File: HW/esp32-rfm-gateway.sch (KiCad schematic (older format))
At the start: 59 parts, among them J1 Res, J2 Boot, J20 220V~, J21 c5V, J22 s14500, J23 s18650, J24 cPS, J25 c3V3, J3 PinDbg, J30 AntSMA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

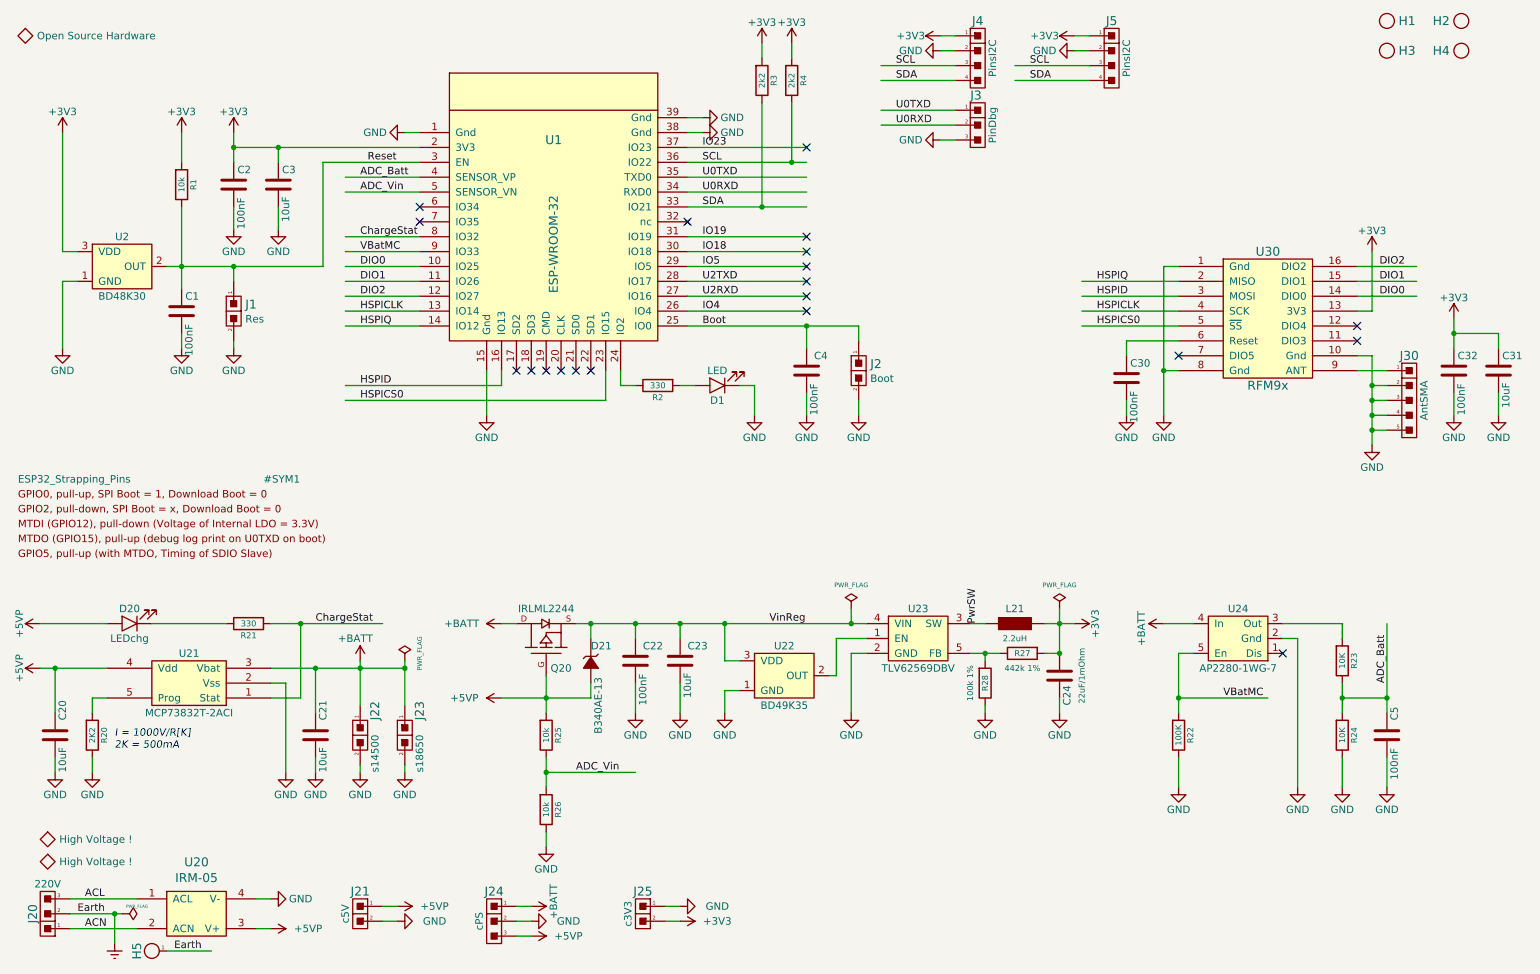
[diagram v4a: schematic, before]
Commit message: Rebuilds the power sections, again ...
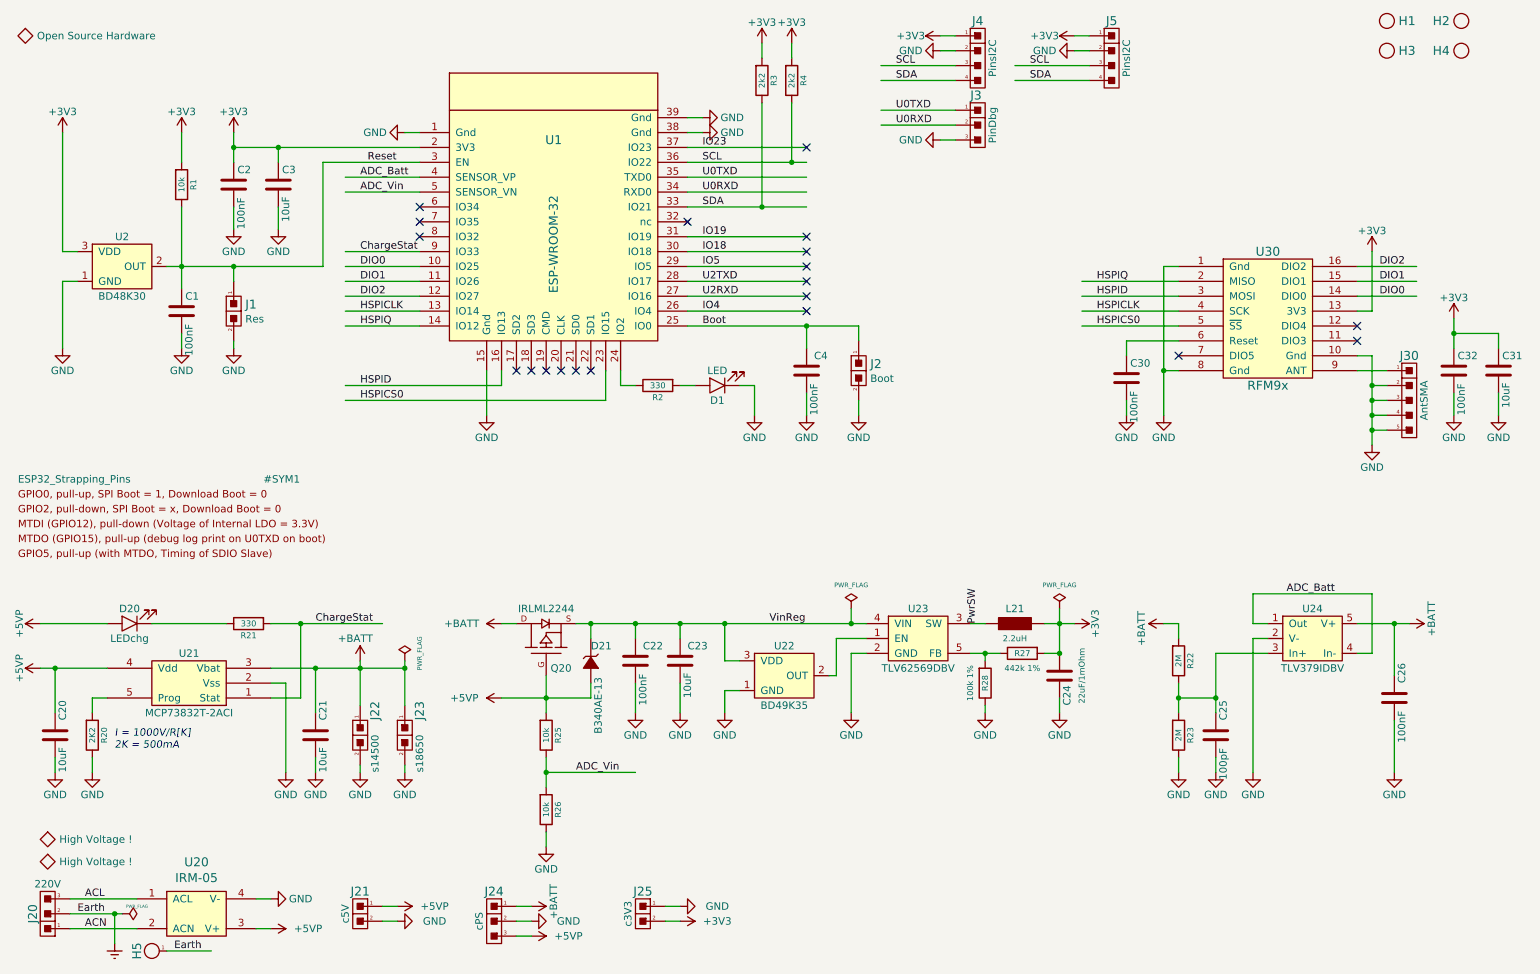
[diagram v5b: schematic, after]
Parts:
- removed R24: 10K, CalinGeneric:R0805HS, symbol calin:R
- removed U24: AP2280-1WG-7, CalinGeneric:SOT-23-5-HS, symbol calin:AP2280-1WG-7
- added C25: 100pF, CalinGeneric:C0805HS, symbol Device:C
- added U24: TLV379IDBV, CalinGeneric:SOT-23-5-HS, symbol calin:TLV379IDBV
- R22: value 100K -> 2M
- R23: value 10K -> 2M
- renumbered C5 to C26
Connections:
- net labels removed: VBatMC
- wire segments 211 -> 214
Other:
- moved on the sheet: C26, R22, R23
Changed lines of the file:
@@
 Title "ESP32 RFM69/RFM9x Gateway"
 Date "2019-04-13"
-Rev "16"
+Rev "17"
 Comp "Calin Radoni"
 Comment1 ""
@@
 	1950 2500 1950 2650
 $Comp
-L calin:R R24
-U 1 1 5C35D5DE
-P 9750 5650
-F 0 "R24" V 9830 5650 40  0000 C CNN
-F 1 "10K" V 9750 5650 40  0000 C CNN
-F 2 "CalinGeneric:R0805HS" V 9680 5650 30  0001 C CNN
-F 3 "" H 9750 5650 30  0000 C CNN
-	1    9750 5650
-	1    0    0    -1
-$EndComp
-$Comp
 L calin:R R23
 U 1 1 5C35D656
-P 9750 5150
-F 0 "R23" V 9830 5150 40  0000 C CNN
-F 1 "10K" V 9750 5150 40  0000 C CNN
-F 2 "CalinGeneric:R0805HS" V 9680 5150 30  0001 C CNN
-F 3 "" H 9750 5150 30  0000 C CNN
-	1    9750 5150
+P 8650 5650
+F 0 "R23" V 8730 5650 40  0000 C CNN
+F 1 "2M" V 8650 5650 40  0000 C CNN
+F 2 "CalinGeneric:R0805HS" V 8580 5650 30  0001 C CNN
+F 3 "" H 8650 5650 30  0000 C CNN
+	1    8650 5650
 	1    0    0    -1
 $EndComp
@@
 	0    -1   -1   0
 $EndComp
-$Comp
-L power:GND #PWR0114
-U 1 1 5C35D729
-P 9750 6000
-F 0 "#PWR0114" H 9750 5750 50  0001 C CNN
-F 1 "GND" H 9750 5850 50  0000 C CNN
-F 2 "" H 9750 6000 50  0000 C CNN
-F 3 "" H 9750 6000 50  0000 C CNN
-	1    9750 6000
-	1    0    0    -1
-$EndComp
-Wire Wire Line
-	9750 5800 9750 6000
-Text Label 10050 5300 1    50   ~ 0
+Text Label 9700 4700 2    50   ~ 0
 ADC_Batt
 Wire Wire Line
@@
 	1    0    0    -1
 $EndComp
-Wire Wire Line
-	3550 2300 3050 2300
 $Comp
 L calin:LED D1
@@
 L power:GND #PWR0125
 U 1 1 5C64E70C
-P 9450 6000
-F 0 "#PWR0125" H 9450 5750 50  0001 C CNN
-F 1 "GND" H 9450 5850 50  0000 C CNN
-F 2 "" H 9450 6000 50  0000 C CNN
-F 3 "" H 9450 6000 50  0000 C CNN
-	1    9450 6000
+P 9150 5900
+F 0 "#PWR0125" H 9150 5650 50  0001 C CNN
+F 1 "GND" H 9150 5750 50  0000 C CNN
+F 2 "" H 9150 5900 50  0000 C CNN
+F 3 "" H 9150 5900 50  0000 C CNN
+	1    9150 5900
 	1    0    0    -1
 $EndComp
@@
 L calin:R R22
 U 1 1 5C6A9C35
-P 8650 5650
-F 0 "R22" V 8730 5650 40  0000 C CNN
-F 1 "100K" V 8650 5650 40  0000 C CNN
-F 2 "CalinGeneric:R0805HS" V 8580 5650 30  0001 C CNN
-F 3 "" H 8650 5650 30  0000 C CNN
-	1    8650 5650
+P 8650 5150
+F 0 "R22" V 8730 5150 40  0000 C CNN
+F 1 "2M" V 8650 5150 40  0000 C CNN
+F 2 "CalinGeneric:R0805HS" V 8580 5150 30  0001 C CNN
+F 3 "" H 8650 5150 30  0000 C CNN
+	1    8650 5150
 	1    0    0    -1
 $EndComp
@@
 L power:GND #PWR0126
 U 1 1 5C68E455
-P 8650 6000
-F 0 "#PWR0126" H 8650 5750 50  0001 C CNN
-F 1 "GND" H 8650 5850 50  0000 C CNN
-F 2 "" H 8650 6000 50  0000 C CNN
-F 3 "" H 8650 6000 50  0000 C CNN
-	1    8650 6000
-	1    0    0    -1
-$EndComp
-Wire Wire Line
-	8650 5800 8650 6000
-$Comp
-L calin:AP2280-1WG-7 U24
-U 1 1 5C6B0532
-P 9050 5000
-F 0 "U24" H 9050 4800 50  0000 C CNN
-F 1 "AP2280-1WG-7" H 9050 5200 50  0000 C CNN
-F 2 "CalinGeneric:SOT-23-5-HS" H 9050 5000 50  0001 C CNN
-F 3 "" H 9050 5000 50  0001 C CNN
-	1    9050 5000
-	-1   0    0    1
-$EndComp
-NoConn ~ 9350 5100
-Wire Wire Line
-	9350 4900 9750 4900
-Wire Wire Line
-	9750 4900 9750 5000
-Wire Wire Line
-	9350 5000 9450 5000
-Wire Wire Line
-	9450 5000 9450 6000
-Wire Wire Line
-	8750 5100 8650 5100
-Wire Wire Line
-	8650 5100 8650 5400
-Wire Wire Line
-	8750 4900 8550 4900
-Wire Wire Line
-	8650 5400 9250 5400
-Connection ~ 8650 5400
-Wire Wire Line
-	8650 5400 8650 5500
-Text Label 8950 5400 0    50   ~ 0
-VBatMC
+P 8650 5900
+F 0 "#PWR0126" H 8650 5650 50  0001 C CNN
+F 1 "GND" H 8650 5750 50  0000 C CNN
+F 2 "" H 8650 5900 50  0000 C CNN
+F 3 "" H 8650 5900 50  0000 C CNN
+	1    8650 5900
+	1    0    0    -1
+$EndComp
 $Comp
 L calin:BD49K U22
@@
 Text Label 6750 1550 0    50   ~ 0
 U0RXD
-Text Label 3150 2400 0    50   ~ 0
-VBatMC
 Wire Wire Line
 	10050 3300 9950 3300
@@
 	9950 3600 9950 3500
 $Comp
-L Device:C C5
+L Device:C C26
 U 1 1 5CD11338
-P 10050 5650
-F 0 "C5" V 10100 5750 50  0000 L CNN
-F 1 "100nF" V 10100 5350 50  0000 L CNN
-F 2 "CalinGeneric:C0805HS" H 10088 5500 50  0001 C CNN
-F 3 "" H 10050 5650 50  0000 C CNN
-	1    10050 5650
-	1    0    0    -1
-$EndComp
-$Comp
-L power:GND #PWR0140
-U 1 1 5CD113F8
-P 10050 6000
-F 0 "#PWR0140" H 10050 5750 50  0001 C CNN
-F 1 "GND" H 10050 5850 50  0000 C CNN
-F 2 "" H 10050 6000 50  0000 C CNN
-F 3 "" H 10050 6000 50  0000 C CNN
-	1    10050 6000
-	1    0    0    -1
-$EndComp
-Wire Wire Line
-	10050 6000 10050 5800
-Wire Wire Line
-	9750 5300 9750 5400
-Wire Wire Line
-	10050 5500 10050 5400
-Wire Wire Line
-	10050 5400 9750 5400
-Connection ~ 9750 5400
-Wire Wire Line
-	9750 5400 9750 5500
-Wire Wire Line
-	10050 5400 10050 4900
-Connection ~ 10050 5400
+P 10100 5400
+F 0 "C26" V 10150 5500 50  0000 L CNN
+F 1 "100nF" V 10150 5100 50  0000 L CNN
+F 2 "CalinGeneric:C0805HS" H 10138 5250 50  0001 C CNN
+F 3 "" H 10100 5400 50  0000 C CNN
+	1    10100 5400
+	1    0    0    -1
+$EndComp
 $Comp
 L calin:CS_3 J20
@@
 Text Label 2850 4900 0    50   ~ 0
 ChargeStat
-Text Label 3150 2300 0    50   ~ 0
-ChargeStat
 $Comp
 L power:PWR_FLAG #FLG0101
@@
 NoConn ~ 3550 2100
 NoConn ~ 3550 2200
+$Comp
+L calin:TLV379IDBV U24
+U 1 1 5CB3BC97
+P 9550 5000
+F 0 "U24" H 9550 5200 50  0000 C CNN
+F 1 "TLV379IDBV" H 9550 4800 50  0000 C CNN
+F 2 "CalinGeneric:SOT-23-5-HS" H 9550 5000 50  0001 C CNN
+F 3 "" H 9550 5000 50  0001 C CNN
+	1    9550 5000
+	1    0    0    -1
+$EndComp
+Wire Wire Line
+	9250 4900 9150 4900
+Wire Wire Line
+	9150 4900 9150 4700
+Wire Wire Line
+	9150 4700 9950 4700
+Wire Wire Line
+	9950 4700 9950 5100
+Wire Wire Line
+	9950 5100 9850 5100
+$Comp
+L Device:C C25
+U 1 1 5CC0DFEC
+P 8900 5650
+F 0 "C25" V 8950 5750 50  0000 L CNN
+F 1 "100pF" V 8950 5350 50  0000 L CNN
+F 2 "CalinGeneric:C0805HS" H 8938 5500 50  0001 C CNN
+F 3 "" H 8900 5650 50  0000 C CNN
+	1    8900 5650
+	1    0    0    -1
+$EndComp
+$Comp
+L power:+BATT #PWR0114
+U 1 1 5CC18EFD
+P 10200 4900
+F 0 "#PWR0114" H 10200 4750 50  0001 C CNN
+F 1 "+BATT" H 10050 5050 50  0000 L CNN
+F 2 "" H 10200 4900 50  0001 C CNN
+F 3 "" H 10200 4900 50  0001 C CNN
+	1    10200 4900
+	0    1    1    0
+$EndComp
+$Comp
+L power:GND #PWR0140
+U 1 1 5CC1963B
+P 8900 5900
+F 0 "#PWR0140" H 8900 5650 50  0001 C CNN
+F 1 "GND" H 8900 5750 50  0000 C CNN
+F 2 "" H 8900 5900 50  0000 C CNN
+F 3 "" H 8900 5900 50  0000 C CNN
+	1    8900 5900
+	1    0    0    -1
+$EndComp
+$Comp
+L power:GND #PWR0149
+U 1 1 5CC19822
+P 10100 5900
+F 0 "#PWR0149" H 10100 5650 50  0001 C CNN
+F 1 "GND" H 10100 5750 50  0000 C CNN
+F 2 "" H 10100 5900 50  0000 C CNN
+F 3 "" H 10100 5900 50  0000 C CNN
+	1    10100 5900
+	1    0    0    -1
+$EndComp
+Wire Wire Line
+	8550 4900 8650 4900
+Wire Wire Line
+	8650 4900 8650 5000
+Wire Wire Line
+	8650 5300 8650 5400
+Wire Wire Line
+	8650 5800 8650 5900
+Wire Wire Line
+	8900 5800 8900 5900
+Wire Wire Line
+	8650 5400 8900 5400
+Wire Wire Line
+	8900 5400 8900 5500
+Connection ~ 8650 5400
+Wire Wire Line
+	8650 5400 8650 5500
+Wire Wire Line
+	9250 5000 9150 5000
+Wire Wire Line
+	9150 5000 9150 5900
+Wire Wire Line
+	9850 4900 10100 4900
+Wire Wire Line
+	10100 5250 10100 4900
+Connection ~ 10100 4900
+Wire Wire Line
+	10100 4900 10200 4900
+Wire Wire Line
+	10100 5550 10100 5900
+Wire Wire Line
+	9250 5100 8900 5100
+Wire Wire Line
+	8900 5100 8900 5400
+Connection ~ 8900 5400
+Text Label 3150 2400 0    50   ~ 0
+ChargeStat
+NoConn ~ 3550 2300
 $EndSCHEMATC

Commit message: Changes the power connector to SMD pins
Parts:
- H5: footprint CalinGeneric:HolePlated-M2.5 -> CalinConnectors:SMD_Pins_Big_1x1
- J20: footprint CalinConnectors:DG301-5-3 -> CalinConnectors:SMD_Pins_Big_1x3
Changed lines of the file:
@@
 Sheet 1 1
 Title "ESP32 RFM69/RFM9x Gateway"
-Date "2019-04-13"
-Rev "17"
+Date "2019-04-14"
+Rev "18"
 Comp "Calin Radoni"
 Comment1 ""
@@
 F 0 "J20" V 1150 6850 60  0000 C CNN
 F 1 "220V~" H 1050 6650 50  0000 C CNN
-F 2 "CalinConnectors:DG301-5-3" H 1050 6950 60  0001 C CNN
+F 2 "CalinConnectors:SMD_Pins_Big_1x3" H 1050 6950 60  0001 C CNN
 F 3 "" H 1050 6950 60  0000 C CNN
 	1    1050 6850
@@
 F 0 "H5" H 1750 7200 60  0000 C CNN
 F 1 "HolePlated" H 1750 7000 60  0001 C CNN
-F 2 "CalinGeneric:HolePlated-M2.5" H 1750 7100 60  0001 C CNN
+F 2 "CalinConnectors:SMD_Pins_Big_1x1" H 1750 7100 60  0001 C CNN
 F 3 "" H 1750 7100 60  0000 C CNN
 	1    1750 7100

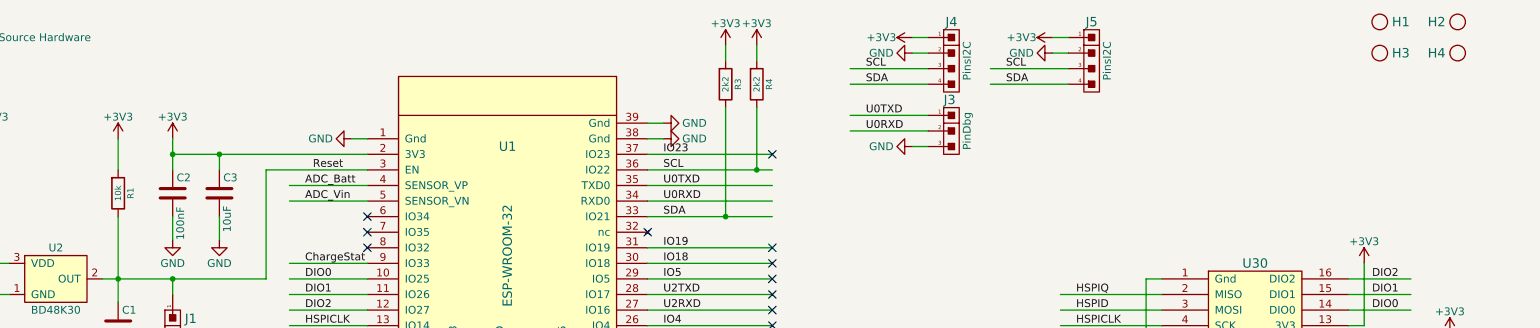
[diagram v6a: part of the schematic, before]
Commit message: Adds CryptoAuthentication device and connects a few more traces
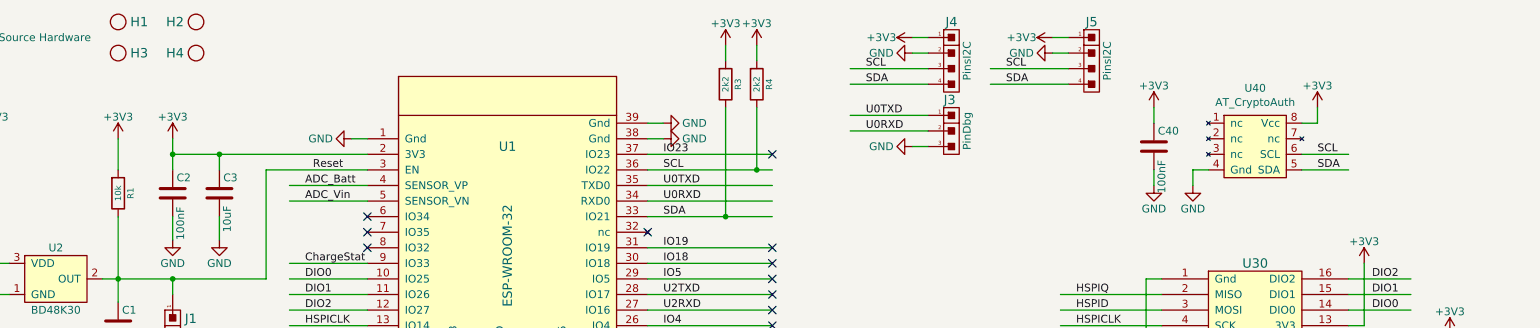
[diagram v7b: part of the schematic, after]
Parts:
- added C40: 100nF, CalinGeneric:C0805HS, symbol Device:C
- added U40: AT_CryptoAuth, CalinGeneric:SOIC-8-HS, symbol calin:AT_CryptoAuth
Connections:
- wire segments 214 -> 222
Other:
- moved on the sheet: H1, H2, H3, H4
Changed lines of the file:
@@
 Title "ESP32 RFM69/RFM9x Gateway"
 Date "2019-04-14"
-Rev "18"
+Rev "19"
 Comp "Calin Radoni"
 Comment1 ""
@@
 L calin:Hole H1
 U 1 1 5C169D3F
-P 10050 850
-F 0 "H1" H 10128 850 60  0000 L CNN
-F 1 "Hole" H 10150 800 60  0001 C CNN
-F 2 "CalinGeneric:HoleNPT-M2.5" H 10050 850 60  0001 C CNN
-F 3 "" H 10050 850 60  0000 C CNN
-	1    10050 850
+P 1950 850
+F 0 "H1" H 2028 850 60  0000 L CNN
+F 1 "Hole" H 2050 800 60  0001 C CNN
+F 2 "CalinGeneric:HoleNPT-M2.5" H 1950 850 60  0001 C CNN
+F 3 "" H 1950 850 60  0000 C CNN
+	1    1950 850
 	1    0    0    -1
 $EndComp
@@
 L calin:Hole H2
 U 1 1 5C169F65
-P 10550 850
-F 0 "H2" H 10628 850 60  0000 L CNN
-F 1 "Hole" H 10650 800 60  0001 C CNN
-F 2 "CalinGeneric:HoleNPT-M2.5" H 10550 850 60  0001 C CNN
-F 3 "" H 10550 850 60  0000 C CNN
-	1    10550 850
+P 2450 850
+F 0 "H2" H 2528 850 60  0000 L CNN
+F 1 "Hole" H 2550 800 60  0001 C CNN
+F 2 "CalinGeneric:HoleNPT-M2.5" H 2450 850 60  0001 C CNN
+F 3 "" H 2450 850 60  0000 C CNN
+	1    2450 850
 	-1   0    0    -1
 $EndComp
@@
 L calin:Hole H3
 U 1 1 5CB3F287
-P 10050 1050
-F 0 "H3" H 10128 1050 60  0000 L CNN
-F 1 "Hole" H 10150 1000 60  0001 C CNN
-F 2 "CalinGeneric:HoleNPT-M2.5" H 10050 1050 60  0001 C CNN
-F 3 "" H 10050 1050 60  0000 C CNN
-	1    10050 1050
+P 1950 1050
+F 0 "H3" H 2028 1050 60  0000 L CNN
+F 1 "Hole" H 2050 1000 60  0001 C CNN
+F 2 "CalinGeneric:HoleNPT-M2.5" H 1950 1050 60  0001 C CNN
+F 3 "" H 1950 1050 60  0000 C CNN
+	1    1950 1050
 	1    0    0    -1
 $EndComp
@@
 L calin:Hole H4
 U 1 1 5CB3F28D
-P 10550 1050
-F 0 "H4" H 10628 1050 60  0000 L CNN
-F 1 "Hole" H 10650 1000 60  0001 C CNN
-F 2 "CalinGeneric:HoleNPT-M2.5" H 10550 1050 60  0001 C CNN
-F 3 "" H 10550 1050 60  0000 C CNN
-	1    10550 1050
+P 2450 1050
+F 0 "H4" H 2528 1050 60  0000 L CNN
+F 1 "Hole" H 2550 1000 60  0001 C CNN
+F 2 "CalinGeneric:HoleNPT-M2.5" H 2450 1050 60  0001 C CNN
+F 3 "" H 2450 1050 60  0000 C CNN
+	1    2450 1050
 	-1   0    0    -1
 $EndComp
@@
 ChargeStat
 NoConn ~ 3550 2300
+$Comp
+L calin:AT_CryptoAuth U40
+U 1 1 5CB52A4F
+P 9250 1650
+F 0 "U40" H 9250 2025 50  0000 C CNN
+F 1 "AT_CryptoAuth" H 9250 1934 50  0000 C CNN
+F 2 "CalinGeneric:SOIC-8-HS" H 9250 1650 50  0001 C CNN
+F 3 "" H 9250 1650 50  0001 C CNN
+	1    9250 1650
+	1    0    0    -1
+$EndComp
+$Comp
+L Device:C C40
+U 1 1 5CB5F1ED
+P 8600 1650
+F 0 "C40" H 8625 1750 50  0000 L CNN
+F 1 "100nF" V 8650 1350 50  0000 L CNN
+F 2 "CalinGeneric:C0805HS" H 8638 1500 50  0001 C CNN
+F 3 "" H 8600 1650 50  0000 C CNN
+	1    8600 1650
+	1    0    0    -1
+$EndComp
+$Comp
+L power:+3V3 #PWR0150
+U 1 1 5CB5F2B7
+P 9650 1400
+F 0 "#PWR0150" H 9650 1250 50  0001 C CNN
+F 1 "+3V3" H 9650 1540 50  0000 C CNN
+F 2 "" H 9650 1400 50  0000 C CNN
+F 3 "" H 9650 1400 50  0000 C CNN
+	1    9650 1400
+	1    0    0    -1
+$EndComp
+$Comp
+L power:+3V3 #PWR0151
+U 1 1 5CB5F338
+P 8600 1400
+F 0 "#PWR0151" H 8600 1250 50  0001 C CNN
+F 1 "+3V3" H 8600 1540 50  0000 C CNN
+F 2 "" H 8600 1400 50  0000 C CNN
+F 3 "" H 8600 1400 50  0000 C CNN
+	1    8600 1400
+	1    0    0    -1
+$EndComp
+$Comp
+L power:GND #PWR0152
+U 1 1 5CB5F3B9
+P 8600 1900
+F 0 "#PWR0152" H 8600 1650 50  0001 C CNN
+F 1 "GND" H 8600 1750 50  0000 C CNN
+F 2 "" H 8600 1900 50  0000 C CNN
+F 3 "" H 8600 1900 50  0000 C CNN
+	1    8600 1900
+	1    0    0    -1
+$EndComp
+Wire Wire Line
+	8600 1400 8600 1500
+Wire Wire Line
+	8600 1800 8600 1900
+Wire Wire Line
+	9650 1400 9650 1500
+Wire Wire Line
+	9650 1500 9550 1500
+$Comp
+L power:GND #PWR0153
+U 1 1 5CB83A79
+P 8850 1900
+F 0 "#PWR0153" H 8850 1650 50  0001 C CNN
+F 1 "GND" H 8850 1750 50  0000 C CNN
+F 2 "" H 8850 1900 50  0000 C CNN
+F 3 "" H 8850 1900 50  0000 C CNN
+	1    8850 1900
+	1    0    0    -1
+$EndComp
+Wire Wire Line
+	8950 1800 8850 1800
+Wire Wire Line
+	8850 1800 8850 1900
+Wire Wire Line
+	9550 1700 9850 1700
+Wire Wire Line
+	9550 1800 9850 1800
+Text Label 9650 1700 0    50   ~ 0
+SCL
+Text Label 9650 1800 0    50   ~ 0
+SDA
 $EndSCHEMATC
